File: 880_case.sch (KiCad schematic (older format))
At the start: 118 parts

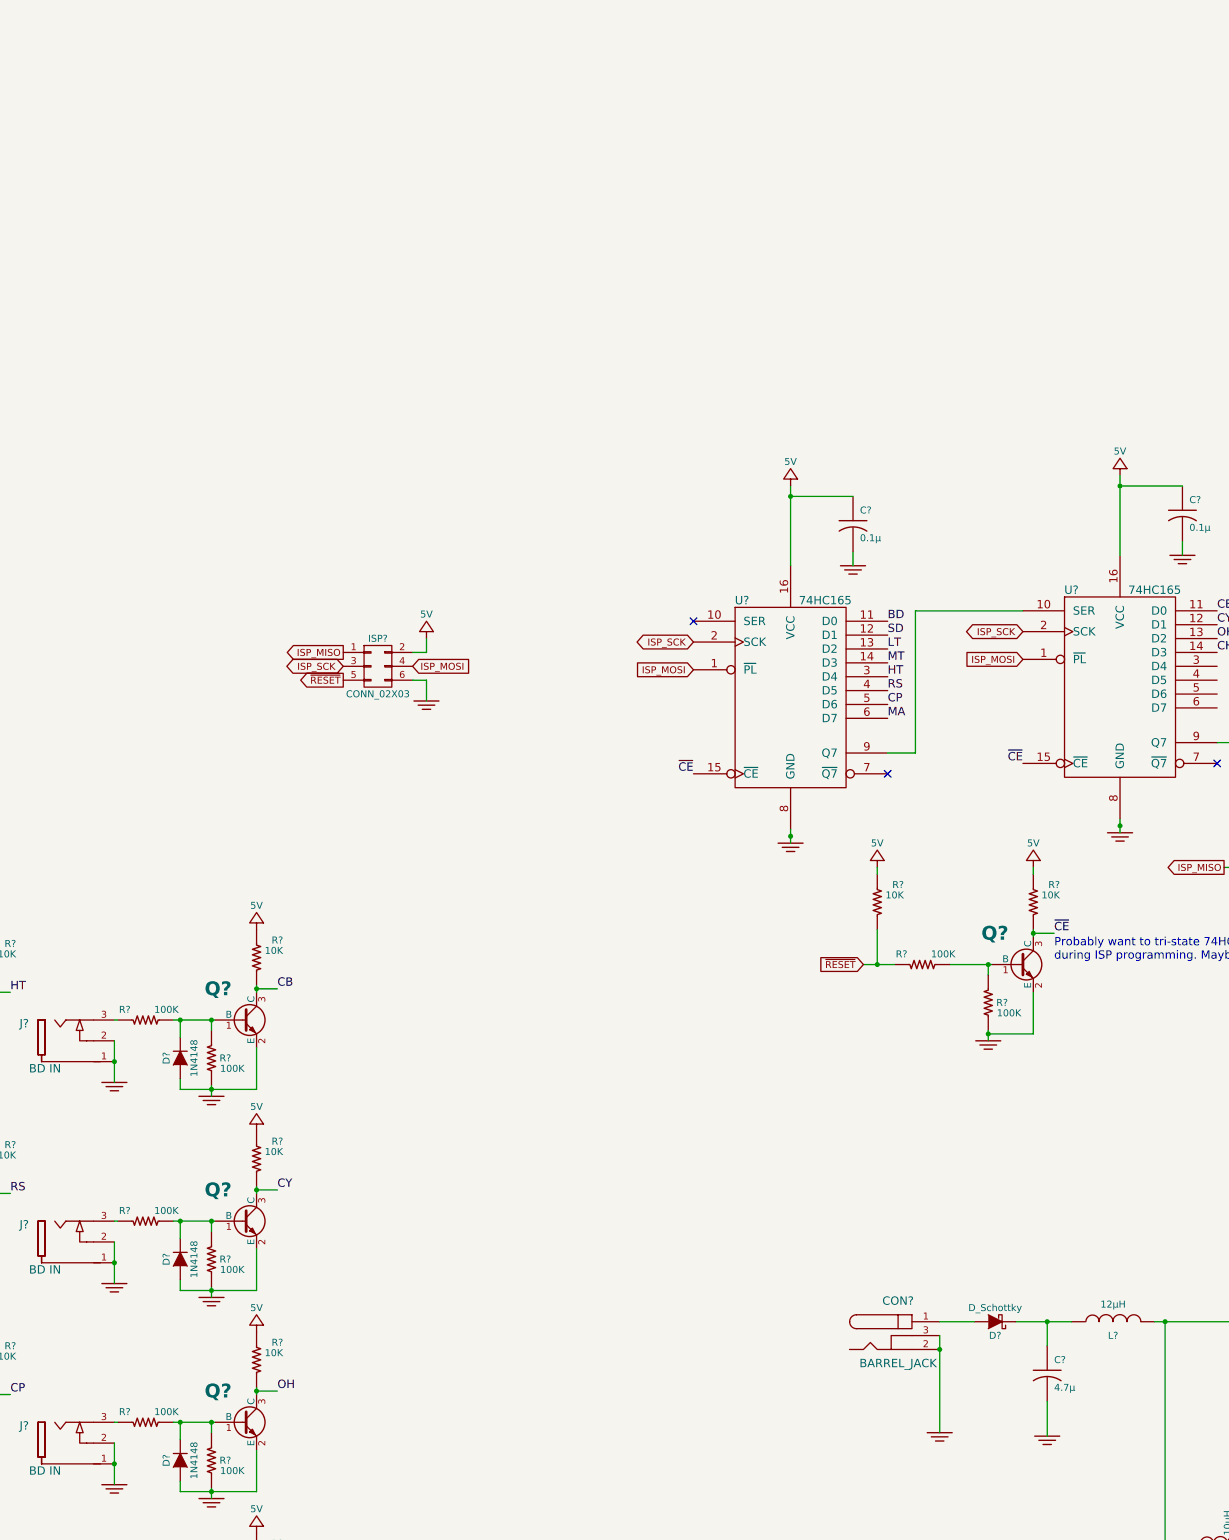
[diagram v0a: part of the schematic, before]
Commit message: added mixer plus balanced out
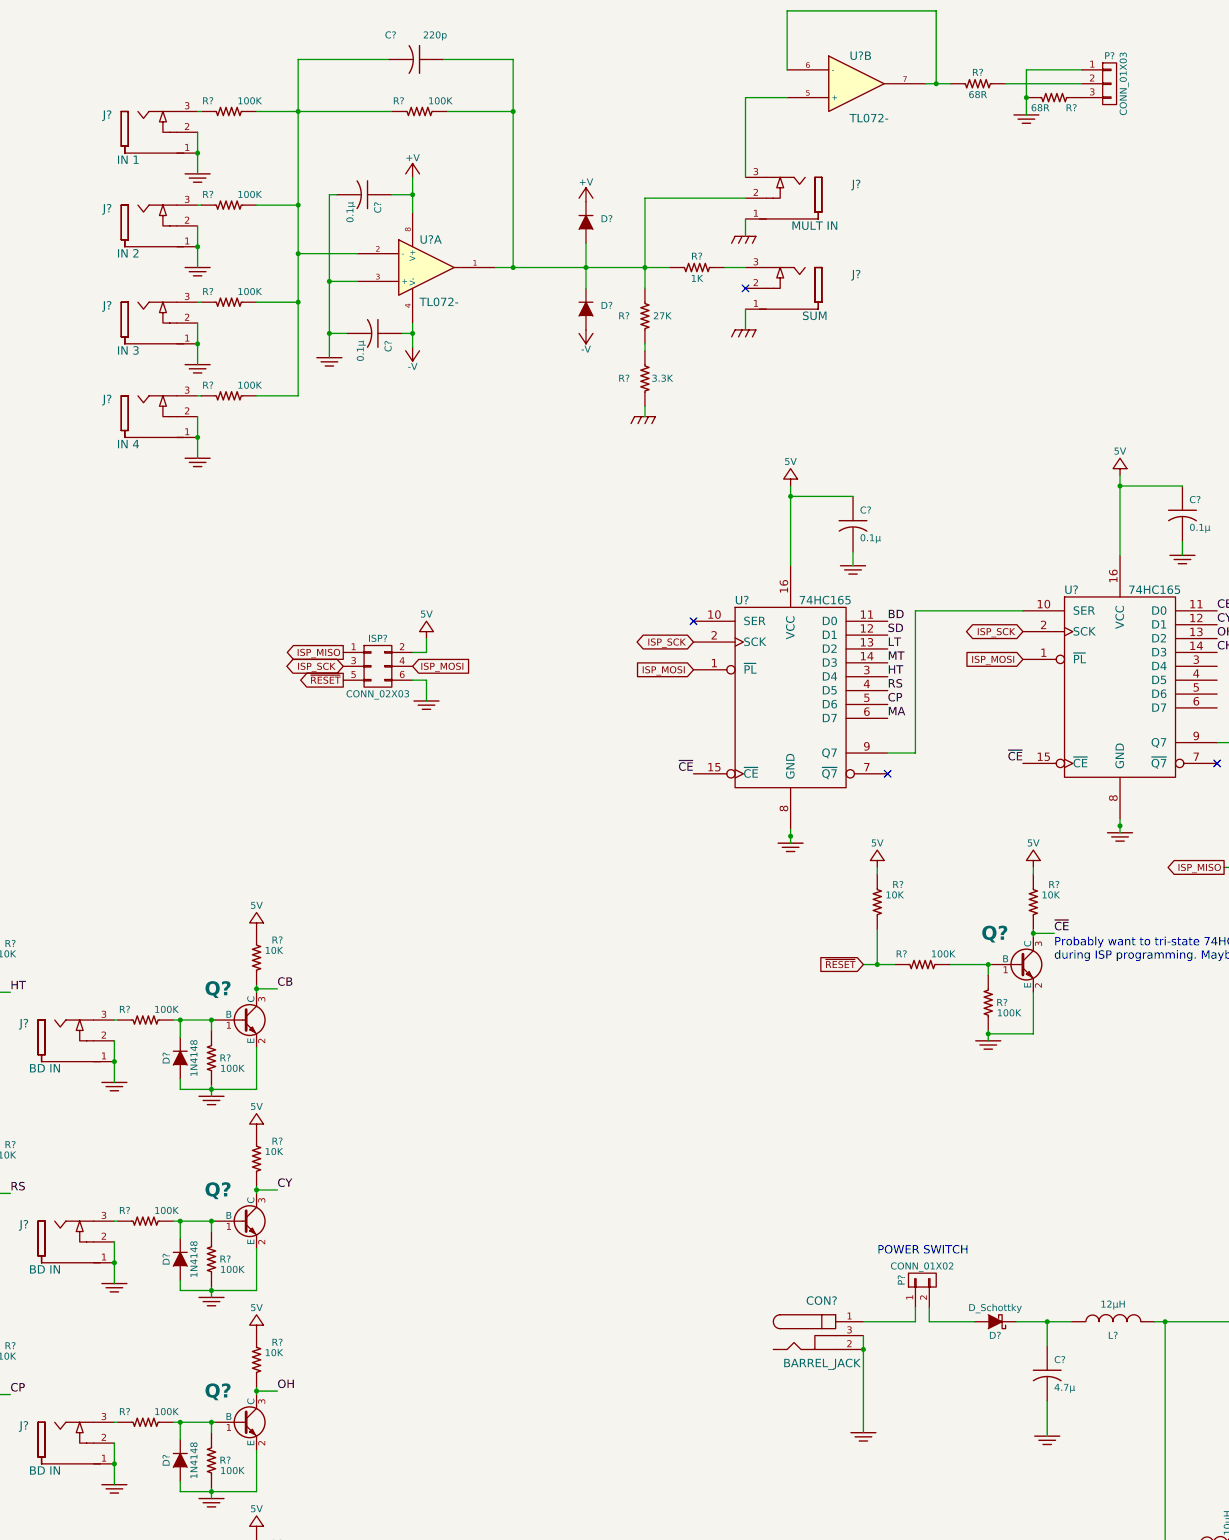
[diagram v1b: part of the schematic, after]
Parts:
- added C? (x2): 0.1µ, MyModules:SM0603-C-MURATA, symbol C_US
- added C?: 220p, MyModules:SM0603-C-MURATA, symbol C_US
- added D? (x2): 1N4148, MyModules:SOD323-C1A2, symbol D
- added J?: IN 1, MyModules:PJ-301B-JACK-SLOTS, symbol JACK_MONO_SW
- added J?: IN 2, MyModules:PJ-301B-JACK-SLOTS, symbol JACK_MONO_SW
- added J?: IN 3, MyModules:PJ-301B-JACK-SLOTS, symbol JACK_MONO_SW
- added J?: IN 4, MyModules:PJ-301B-JACK-SLOTS, symbol JACK_MONO_SW
- added J?: SUM, MyModules:PJ-301B-JACK-SLOTS, symbol JACK_MONO_SW
- added J?: MULT IN, MyModules:PJ-301B-JACK-SLOTS, symbol JACK_MONO_SW
- added P?: CONN_01X02, symbol CONN_01X02
- added P?: CONN_01X03, symbol CONN_01X03
- added R? (x5): 100K, MyModules:SM0603-R-JRL, symbol R_US
- added R?: 1K, MyModules:SM0603-R-JRL, symbol R_US
- added R?: 27K, MyModules:SM0603-R-JRL, symbol R_US
- added R?: 3.3K, MyModules:SM0603-R-JRL, symbol R_US
- added R? (x2): 68R, MyModules:SM0603-R-JRL, symbol R_US
- added U? (x2): TL072-, symbol TL072-
- C?: footprint MyModules:SM0603-C-JRL -> MyModules:SM0603-C-MURATA
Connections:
- net +V: now also C?.1, D?.1 (K), U?.8 (V+)
- net -V: now also C?.1, D?.2 (A), U?.4 (V-)
- net GND: now also C?.2, C?.2, J?.1, J?.1, J?.1, J?.1, J?.1, J?.1, J?.2, J?.2, J?.2, J?.2, P?.1 (P1), R?.1, R?.2, U?.3 (+)
- net at CON?.1: now also P?.1 (P1); no longer D?.2 (A)
- new net: D?.2 (A), P?.2 (P2)
- new net: P?.2 (P2), R?.1
- new net: P?.3 (P3), R?.1
- new net: J?.3, R?.1 (x5)
- new net: C?.2, R?.1, R?.2, R?.2, R?.2, R?.2, U?.2 (-)
- new net: C?.1, D?.1 (K), D?.2 (A), J?.2, R?.2, R?.2, R?.2, U?.1
- new net: R?.1, R?.2
- new net: J?.3, U?.5 (+)
- new net: R?.2, U?.6 (-), U?.7
- no-connect marks 13 -> 14
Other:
- note added: "POWER SWITCH"
- moved on the sheet: CON?

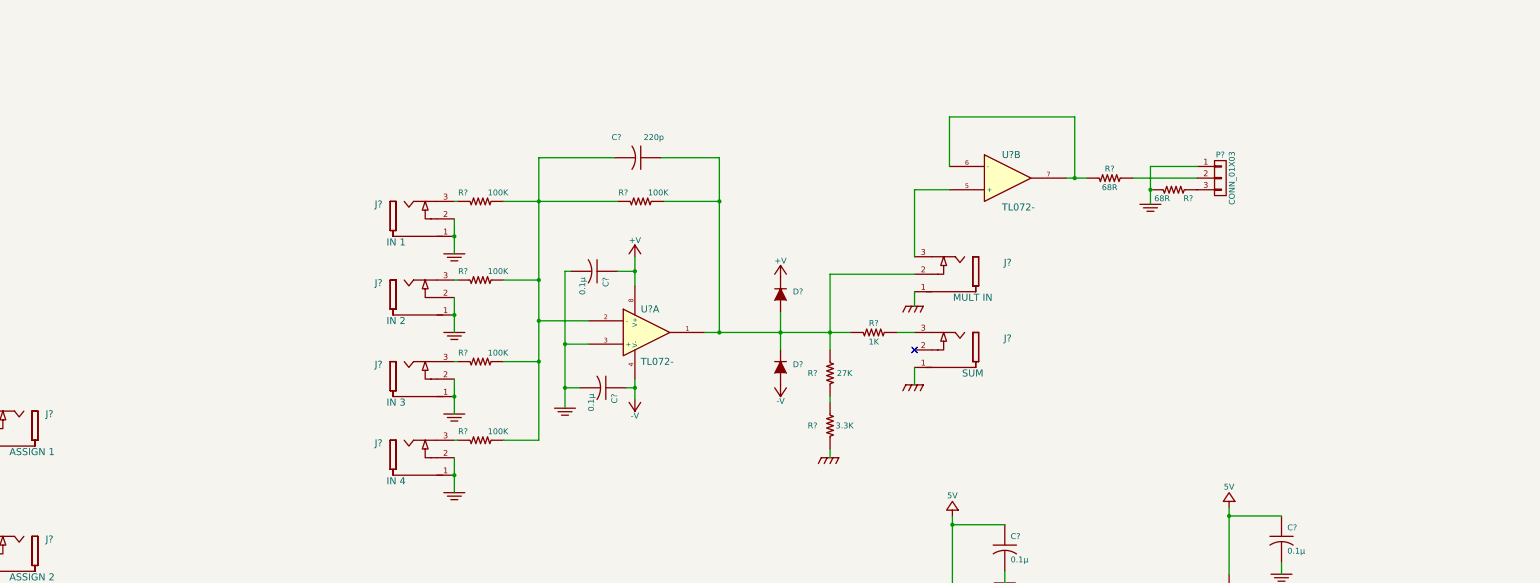
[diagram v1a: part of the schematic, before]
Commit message: added headphone output
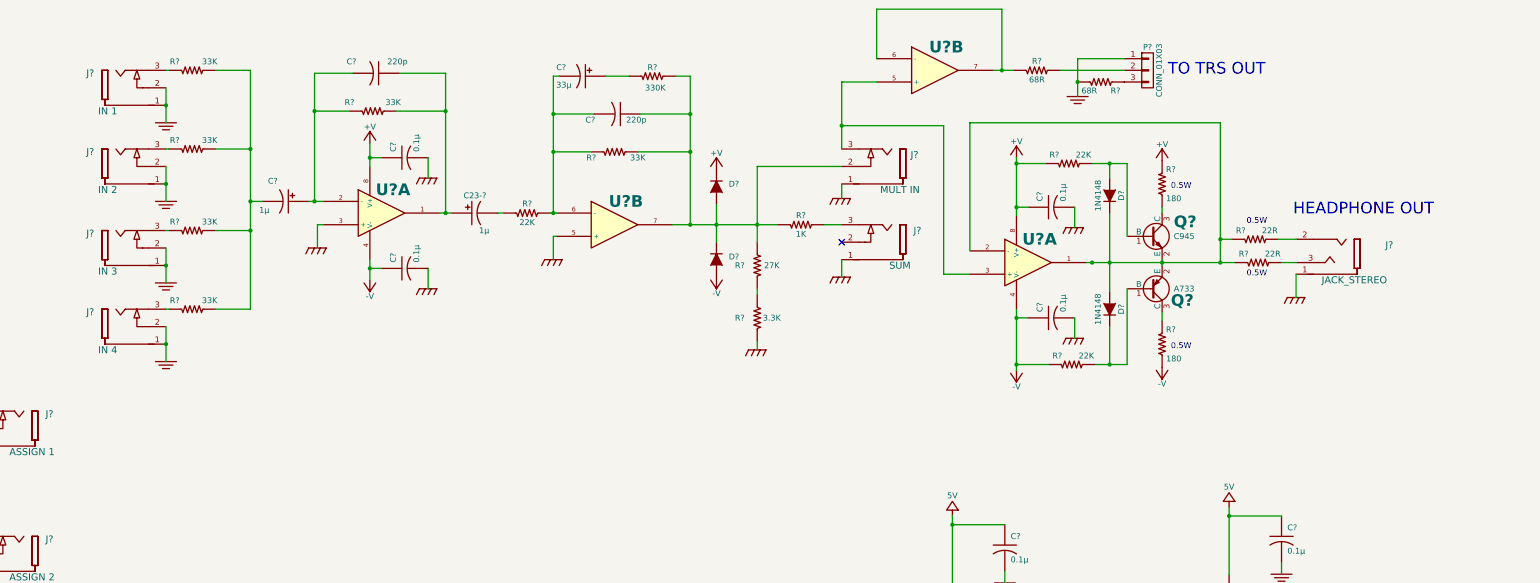
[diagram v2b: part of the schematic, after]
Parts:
- removed C?: 0.1µ, MyModules:SM0603-C-MURATA, symbol C_US
- removed C?: 220p, MyModules:SM0603-C-MURATA, symbol C_US
- removed D? (x2): 1N4148, MyModules:SOD323-C1A2, symbol D
- removed R?: 100K, MyModules:SM0603-R-JRL, symbol R_US
- removed U? (x2): TL072-, symbol TL072-
- added C23-?, C?: 1μ, Capacitors_SMD:c_elec_4x5.3, symbol CP_US
- added C? (x2): 220p, MyModules:SM0603-C-JRL, symbol C_US
- added C?: 33μ, Capacitors_SMD:c_elec_5x5.3, symbol CP_US
- added C? (x3): 0.1µ, MyModules:SM0603-C-MURATA, symbol C_US
- added D? (x4): 1N4148, MyModules:SOD323-C1A2, symbol D
- added J?: JACK_STEREO, symbol JACK_STEREO
- added Q?: C945, SOT-23, symbol C945
- added Q?: A733, SOT-23, symbol A733
- added R? (x2): 33K, MyModules:SM0603-R-JRL, symbol R_US
- added R? (x3): 22K, MyModules:SM0603-R-JRL, symbol R_US
- added R?: 330K, MyModules:SM0603-R-JRL, symbol R_US
- added R? (x2): 180, MyModules:SM0603-R-JRL, symbol R_US
- added R? (x2): 22R, MyModules:SM0603-R-JRL, symbol R_US
- added U? (x4): 4558, MyModules:TSSOP8-JRL, symbol TL072-
- R? (x4): value 100K -> 33K
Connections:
- net +V: now also C?.1, D?.1 (K), R?.1, R?.1, U?.8 (V+), U?.8 (V+)
- net -V: now also C?.1, C?.1, D?.2 (A), R?.1, R?.2, U?.4 (V-), U?.4 (V-)
- net GND: now also C?.2, C?.2, C?.2, J?.1, U?.3 (+), U?.5 (+)
- net at R?.2, R?.2, R?.2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: now also C?.2 (-)
- net at J?.2, R?.2, R?.2: now also C?.1, D?.1 (K), D?.2 (A), R?.2, R?.2, U?.7
- net at J?.3: now also U?.3 (+), U?.5 (+)
- net at R?.2: now also U?.6 (-), U?.7
- new net: C23-?.1 (+), C?.1, R?.2, U?.1
- new net: C?.1 (+), C?.2, R?.1, U?.2 (-)
- new net: C?.2, C?.2 (-), R?.1, R?.2, U?.6 (-)
- new net: C23-?.2 (-), R?.1
- new net: C?.1 (+), R?.1
- new net: J?.2, R?.2
- new net: J?.3, R?.2
- new net: D?.1 (K), D?.2 (A), Q?.2 (E), Q?.2 (E), R?.1, R?.1, U?.1, U?.2 (-)
- new net: D?.2 (A), Q?.1 (B), R?.2
- new net: D?.1 (K), Q?.1 (B), R?.2
- new net: Q?.3 (C), R?.2
- new net: Q?.3 (C), R?.1
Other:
- note added: "0.5W"
- note added: "HEADPHONE OUT"
- note added: "TO TRS OUT"
- moved on the sheet: C?, J?, P?, R?

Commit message: schematic complete, about to do erc and export netlist
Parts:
- J?: value BD IN -> LT IN
- J?: value BD IN -> MT IN
- J?: value BD IN -> HT IN
- J?: value BD IN -> RS IN
- J?: value BD IN -> CP IN
- J?: value BD IN -> MA IN
- J?: value BD IN -> CB IN
- J?: value BD IN -> CY IN
- J?: value BD IN -> OH IN
- J?: value BD IN -> CH IN
- J?: footprint (none) -> MyModules:SJ1-3523N
- P?: footprint DIY:PIN_ARRAY_3X2 -> w_conn_strip:vasch_strip_3x2
- P?: footprint Pin_Headers:Pin_Header_Straight_2x05 -> w_conn_strip:vasch_strip_5x2
- P?: footprint (none) -> Pin_Headers:Pin_Header_Straight_1x02_Pitch2.54mm
- P?: footprint (none) -> Pin_Headers:Pin_Header_Straight_1x03_Pitch2.54mm
- R? (x4): footprint MyModules:SM0603-R-JRL -> Resistors_SMD:R_0805
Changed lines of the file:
@@
 F 0 "P?" H 5675 8400 50  0000 C CNN
 F 1 "CONN_02X03" H 5675 8000 50  0000 C CNN
-F 2 "DIY:PIN_ARRAY_3X2" H 5675 7850 60  0001 C CNN
+F 2 "w_conn_strip:vasch_strip_3x2" H 5675 7850 60  0001 C CNN
 F 3 "" H 5675 7000 60  0000 C CNN
 	1    5675 8200
@@
 F 0 "P?" H 21575 13250 50  0000 C CNN
 F 1 "CONN_02X05" H 21575 12650 50  0000 C CNN
-F 2 "Pin_Headers:Pin_Header_Straight_2x05" H 21575 11750 60  0001 C CNN
+F 2 "w_conn_strip:vasch_strip_5x2" H 21575 11750 60  0001 C CNN
 F 3 "" H 21575 11750 60  0000 C CNN
 	1    21575 12950
@@
 P 5750 13000
 F 0 "J?" H 5350 12875 60  0000 C CNN
-F 1 "BD IN" H 5500 13200 60  0000 C CNN
+F 1 "LT IN" H 5500 13200 60  0000 C CNN
 F 2 "MyModules:PJ-301B-JACK-SLOTS" H 5650 13000 60  0001 C CNN
 F 3 "" H 5650 13000 60  0000 C CNN
@@
 P 5750 14450
 F 0 "J?" H 5350 14325 60  0000 C CNN
-F 1 "BD IN" H 5500 14650 60  0000 C CNN
+F 1 "MT IN" H 5500 14650 60  0000 C CNN
 F 2 "MyModules:PJ-301B-JACK-SLOTS" H 5650 14450 60  0001 C CNN
 F 3 "" H 5650 14450 60  0000 C CNN
@@
 P 7825 10100
 F 0 "J?" H 7425 9975 60  0000 C CNN
-F 1 "BD IN" H 7575 10300 60  0000 C CNN
+F 1 "HT IN" H 7575 10300 60  0000 C CNN
 F 2 "MyModules:PJ-301B-JACK-SLOTS" H 7725 10100 60  0001 C CNN
 F 3 "" H 7725 10100 60  0000 C CNN
@@
 P 7825 11550
 F 0 "J?" H 7425 11425 60  0000 C CNN
-F 1 "BD IN" H 7575 11750 60  0000 C CNN
+F 1 "RS IN" H 7575 11750 60  0000 C CNN
 F 2 "MyModules:PJ-301B-JACK-SLOTS" H 7725 11550 60  0001 C CNN
 F 3 "" H 7725 11550 60  0000 C CNN
@@
 P 7825 13000
 F 0 "J?" H 7425 12875 60  0000 C CNN
-F 1 "BD IN" H 7575 13200 60  0000 C CNN
+F 1 "CP IN" H 7575 13200 60  0000 C CNN
 F 2 "MyModules:PJ-301B-JACK-SLOTS" H 7725 13000 60  0001 C CNN
 F 3 "" H 7725 13000 60  0000 C CNN
@@
 P 7825 14450
 F 0 "J?" H 7425 14325 60  0000 C CNN
-F 1 "BD IN" H 7575 14650 60  0000 C CNN
+F 1 "MA IN" H 7575 14650 60  0000 C CNN
 F 2 "MyModules:PJ-301B-JACK-SLOTS" H 7725 14450 60  0001 C CNN
 F 3 "" H 7725 14450 60  0000 C CNN
@@
 P 9750 10075
 F 0 "J?" H 9350 9950 60  0000 C CNN
-F 1 "BD IN" H 9500 10275 60  0000 C CNN
+F 1 "CB IN" H 9500 10275 60  0000 C CNN
 F 2 "MyModules:PJ-301B-JACK-SLOTS" H 9650 10075 60  0001 C CNN
 F 3 "" H 9650 10075 60  0000 C CNN
@@
 P 9750 11525
 F 0 "J?" H 9350 11400 60  0000 C CNN
-F 1 "BD IN" H 9500 11725 60  0000 C CNN
+F 1 "CY IN" H 9500 11725 60  0000 C CNN
 F 2 "MyModules:PJ-301B-JACK-SLOTS" H 9650 11525 60  0001 C CNN
 F 3 "" H 9650 11525 60  0000 C CNN
@@
 P 9750 12975
 F 0 "J?" H 9350 12850 60  0000 C CNN
-F 1 "BD IN" H 9500 13175 60  0000 C CNN
+F 1 "OH IN" H 9500 13175 60  0000 C CNN
 F 2 "MyModules:PJ-301B-JACK-SLOTS" H 9650 12975 60  0001 C CNN
 F 3 "" H 9650 12975 60  0000 C CNN
@@
 P 9750 14425
 F 0 "J?" H 9350 14300 60  0000 C CNN
-F 1 "BD IN" H 9500 14625 60  0000 C CNN
+F 1 "CH IN" H 9500 14625 60  0000 C CNN
 F 2 "MyModules:PJ-301B-JACK-SLOTS" H 9650 14425 60  0001 C CNN
 F 3 "" H 9650 14425 60  0000 C CNN
@@
 F 0 "P?" H 15825 11950 50  0000 C CNN
 F 1 "CONN_01X02" V 15925 11800 50  0000 C CNN
-F 2 "" H 15825 11800 60  0000 C CNN
+F 2 "Pin_Headers:Pin_Header_Straight_1x02_Pitch2.54mm" H 15825 11800 60  0001 C CNN
 F 3 "" H 15825 11800 60  0000 C CNN
 	1    15825 11800
@@
 F 0 "P?" H 16550 2450 50  0000 C CNN
 F 1 "CONN_01X03" V 16650 2250 50  0000 C CNN
-F 2 "" H 16550 2250 60  0000 C CNN
+F 2 "Pin_Headers:Pin_Header_Straight_1x03_Pitch2.54mm" H 16550 2250 60  0001 C CNN
 F 3 "" H 16550 2250 60  0000 C CNN
 	1    16550 2250
@@
 F 0 "J?" H 17525 3750 60  0000 C CNN
 F 1 "JACK_STEREO" H 17825 4050 60  0000 C CNN
-F 2 "" H 17975 3850 60  0000 C CNN
+F 2 "MyModules:SJ1-3523N" H 17975 3850 60  0001 C CNN
 F 3 "" H 17975 3850 60  0000 C CNN
 	1    18075 3850
@@
 F 0 "R?" H 16750 3350 50  0000 C CNN
 F 1 "180" H 16775 3100 50  0000 C CNN
-F 2 "MyModules:SM0603-R-JRL" H 16675 3225 60  0001 C CNN
+F 2 "Resistors_SMD:R_0805" H 16675 3225 60  0001 C CNN
 F 3 "" H 16675 3225 60  0000 C CNN
 	1    16675 3225
@@
 F 0 "R?" H 16750 4725 50  0000 C CNN
 F 1 "180" H 16775 4475 50  0000 C CNN
-F 2 "MyModules:SM0603-R-JRL" H 16675 4600 60  0001 C CNN
+F 2 "Resistors_SMD:R_0805" H 16675 4600 60  0001 C CNN
 F 3 "" H 16675 4600 60  0000 C CNN
 	1    16675 4600
@@
 F 0 "R?" V 17550 3825 50  0000 C CNN
 F 1 "22R" V 17550 3575 50  0000 C CNN
-F 2 "MyModules:SM0603-R-JRL" H 17475 3700 60  0001 C CNN
+F 2 "Resistors_SMD:R_0805" H 17475 3700 60  0001 C CNN
 F 3 "" H 17475 3700 60  0000 C CNN
 	1    17475 3700
@@
 F 0 "R?" V 17575 4025 50  0000 C CNN
 F 1 "22R" V 17575 3775 50  0000 C CNN
-F 2 "MyModules:SM0603-R-JRL" H 17500 3900 60  0001 C CNN
+F 2 "Resistors_SMD:R_0805" H 17500 3900 60  0001 C CNN
 F 3 "" H 17500 3900 60  0000 C CNN
 	1    17500 3900

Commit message: started layout
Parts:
- C1, C12, C16, C2: renamed from C?; footprint MyModules:SM0603-C-JRL -> MyModules:SM0603-C-MURATA
- C11: renamed from C?; footprint Capacitors_SMD:c_elec_4x5.3 -> Capacitors_SMD:CP_Elec_4x5.3
- C15: renamed from C?; footprint Capacitors_SMD:c_elec_5x5.3 -> Capacitors_SMD:CP_Elec_5x5.3
- C23: renamed from C23-?; footprint Capacitors_SMD:c_elec_4x5.3 -> Capacitors_SMD:CP_Elec_4x5.3
- CON1: renamed from CON?; footprint (none) -> MyModules:712A-DC-JACK
- D17: renamed from D?; footprint (none) -> MyModules:SMB-1C2A
- Q14, Q15: renamed from Q?; footprint SOT-23 -> TO_SOT_Packages_SMD:SOT-23
- R10, R11, R12, R13, R14, R15, R16, R17, R18, R19, R2, R20, R21, R22, R23, R24, R25, R26, R27, R28, R29, R30, R31, R32, R33, R34, R35, R36, R37, R38, R39, R40, R41, R42, R43, R44, R45, R46, R47, R48, R49, R50, R51, R52, R53, R54, R55, R56, R57, R58, R59, R6, R60, R7, R8, R9: renamed from R?; footprint MyModules:SM0603-R-JRL -> MyModules:SM0603-R-YAGEO
- U5, U6: renamed from U?; footprint MyModules:TSSOP8-JRL -> Housings_SSOP:TSSOP-8_3x3mm_Pitch0.65mm
- gave numbers to parts that had none: 94
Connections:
- net +V: now also U6.8 (V+); no longer U6.8 (V+)
- net -V: now also P3.1 (P1), P3.2 (P2), U6.4 (V-); no longer U6.4 (V-)
- net GND: now also P3.4 (P4), P3.6 (P6), P3.8 (P8); no longer P3.1 (P1), P3.2 (P2)
- net at D20.1 (K), D21.2 (A), Q14.2 (E)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: now also U6.1, U6.2 (-); no longer U6.1, U6.2 (-)
- new net: J21.3, U6.3 (+), U6.5 (+)
- new net: R57.2, U6.6 (-), U6.7
- no-connect marks 14 -> 18
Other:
- moved on the sheet: C10, C11, C12, C13, C14, C15, C16, C17, C18, C23, C4, C5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
